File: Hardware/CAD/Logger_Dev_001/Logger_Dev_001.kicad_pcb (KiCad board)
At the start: 4 copper layers, 54.5 x 67 mm, 72 parts, among them J1 Conn_Coaxial, J3 Micro_SD_Card_Det1, J4 Connector, USB-TYPE-C-16P, Q1 BC847BS, Q2 MMBT3904, U1 L76-M33, U2 ESP32-C6-WROOM-1, U5 AMS1117, U6 CP2102-GMR

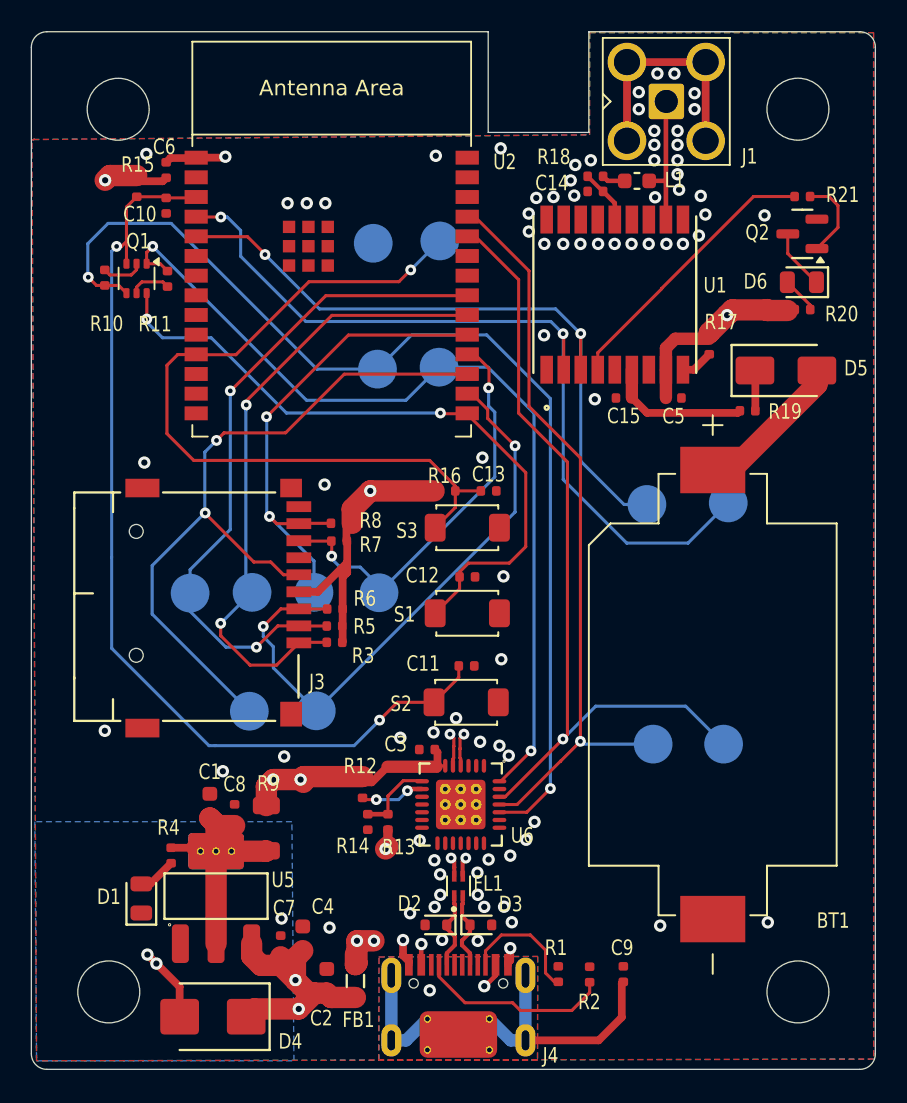
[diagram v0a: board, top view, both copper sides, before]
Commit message: Updated PCB to include strapping pin and USB C DP reroute
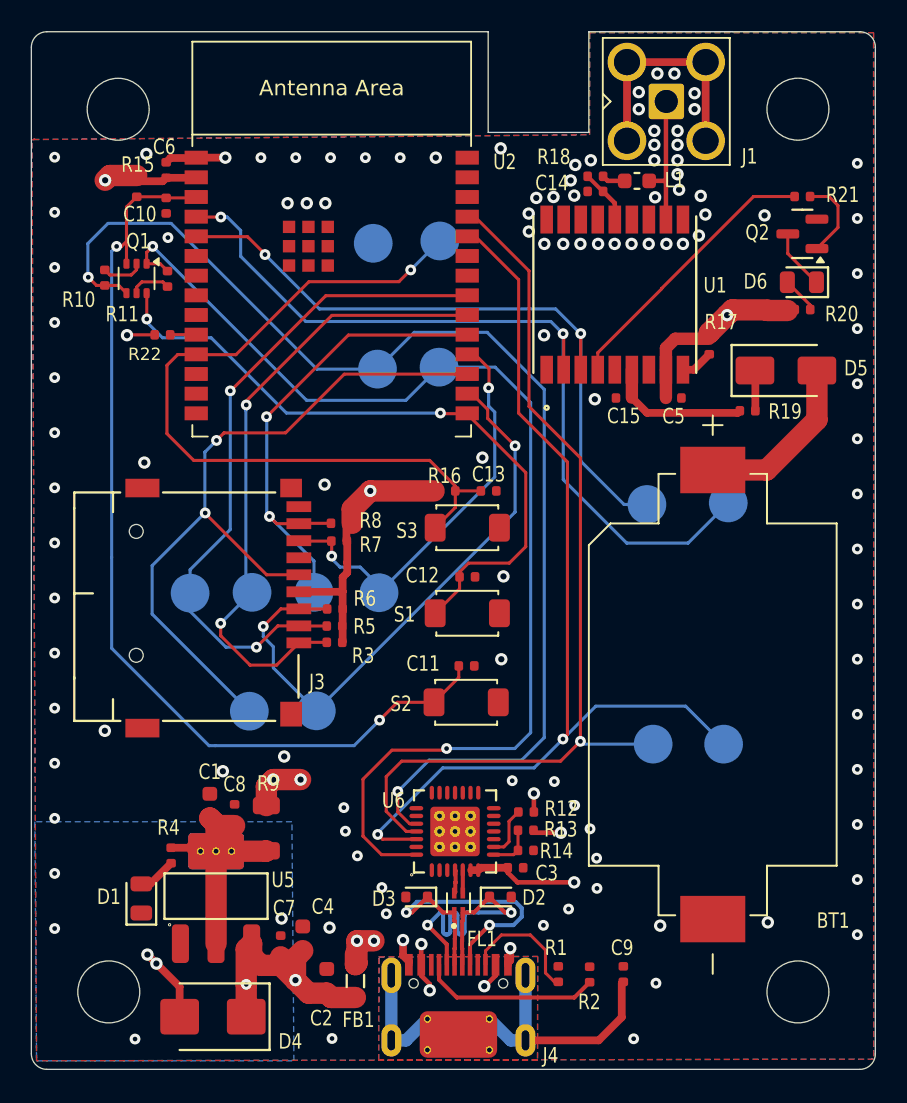
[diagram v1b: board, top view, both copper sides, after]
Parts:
- added R22: 3.3kΩ, PCM_JLCPCB:R_0402, F.Cu at (127.2, 91.5)
- moved R12 10.7 mm to (150.7, 122.3), turned to 180 degrees
- moved R14 10.4 mm to (150.7, 124.8), turned to 0 degrees
- moved C3 9.53 mm to (150.0, 125.9), turned to 0 degrees
- moved R13 8.92 mm to (150.7, 123.5), turned to 180 degrees
- moved D2 4.53 mm to (149.1, 127.8), turned to 0 degrees
- moved D3 4.52 mm to (143.7, 127.8), turned to 180 degrees
- moved U6 1.78 mm to (146.1, 123.5), turned to 0 degrees
- moved FL1 1.09 mm to (146.4, 128.1)
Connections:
- FL1 pad 1: /USB C COMs 3v3 Power Input Module/USB_UNF_D- -> /USB C COMs 3v3 Power Input Module/USB_UNF_D+
- FL1 pad 2: /USB C COMs 3v3 Power Input Module/USB_D- -> /USB C COMs 3v3 Power Input Module/USB_D+
- FL1 pad 3: /USB C COMs 3v3 Power Input Module/USB_D+ -> /USB C COMs 3v3 Power Input Module/USB_D-
- FL1 pad 4: /USB C COMs 3v3 Power Input Module/USB_UNF_D+ -> /USB C COMs 3v3 Power Input Module/USB_UNF_D-
- U2 pad 10: unconnected-(U2-GPIO8-Pad10) -> /STRAP_PIN
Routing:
- net VUSB: track 17.6 -> 41.3 mm
- net /USB C COMs 3v3 Power Input Module/USB_UNF_D+: track 5.13 -> 21.2 mm, vias 0 -> 2
- net /USB C COMs 3v3 Power Input Module/USB_UNF_D-: track 5.13 -> 21.2 mm, vias 0 -> 2
- net /USB C COMs 3v3 Power Input Module/DTR: track 58.4 -> 74.3 mm
- net /USB C COMs 3v3 Power Input Module/USB_D-: track 17.1 -> 1.48 mm, vias 2 -> 0
- net /USB C COMs 3v3 Power Input Module/USB_D+: track 17.0 -> 1.54 mm, vias 2 -> 0
- net /USBC_TX: track 53.5 -> 65.1 mm, vias 1 -> 2
- net /USBC_RX: track 48.9 -> 60.2 mm
- net /USB C COMs 3v3 Power Input Module/RTS: track 71.1 -> 77.7 mm
- net Net-(U6-VBUS): track 5.10 -> 2.98 mm
- net VUSB_UNFILTERD: track 6.42 -> 8.29 mm
- net /STRAP_PIN: track 0.00 -> 1.69 mm
- net Net-(BT1-PadP): track 9.91 -> 11.2 mm
- net Net-(J4-CC1): track 12.5 -> 11.6 mm
- net Net-(U6-RST#): track 4.17 -> 3.30 mm, vias 2 -> 0
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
